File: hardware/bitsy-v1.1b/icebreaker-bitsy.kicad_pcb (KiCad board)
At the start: 4 copper layers, 35.6 x 18 mm, 99 parts, among them J1 USB_C, P0 0, P1 1, P10 10, P11 11, P12 12, P13 13, P14 14, P15 15, P16 16, P17 17, P18 18, P19 19, P2 2, P20 20, P21 21, P22 22, P23 23, P24 GND, P25 GND, P26 GND, P27 3V3, P28 3V3, P29 VIN, P3 3, P30 CDONE, P31 CRESET, P32 UP, P33 UP, P34 UP, P35 UP, P36 CS, P37 SCK, P38 MISO, P39 MOSI, P4 4, P40 IO3, P41 IO2, P5 5, P6 6, P7 7, P8 8, P9 9, SW1 TACT, U1 USBLC6-2, U2 TLV75533PDRV, U3 TLV75512PDRV, U4 LY68L6400, U5 W25Q128JVxxM, U6 ICE40UP5K-SG48, X1 12MHz

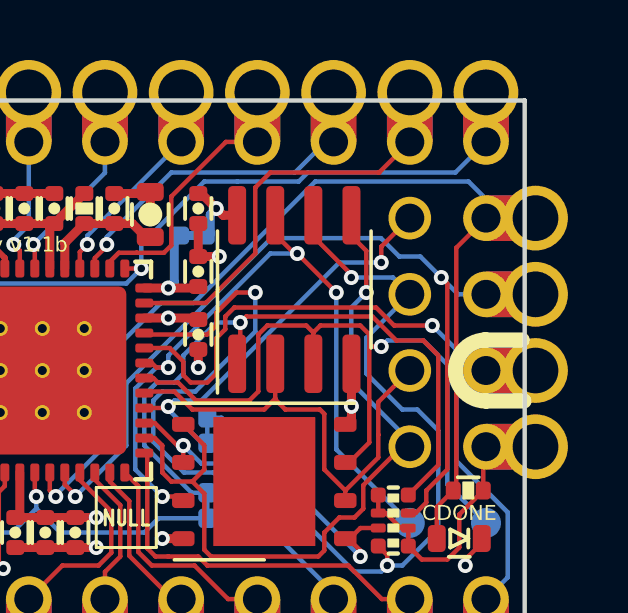
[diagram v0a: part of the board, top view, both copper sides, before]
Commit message: iCEBitsy v1.1b: Add prog header silkscreen labels
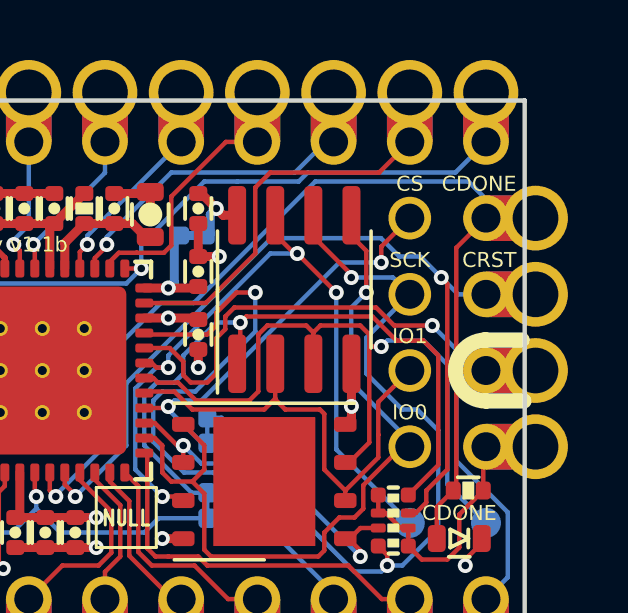
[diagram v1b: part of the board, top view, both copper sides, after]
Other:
- board text added: "CRST"

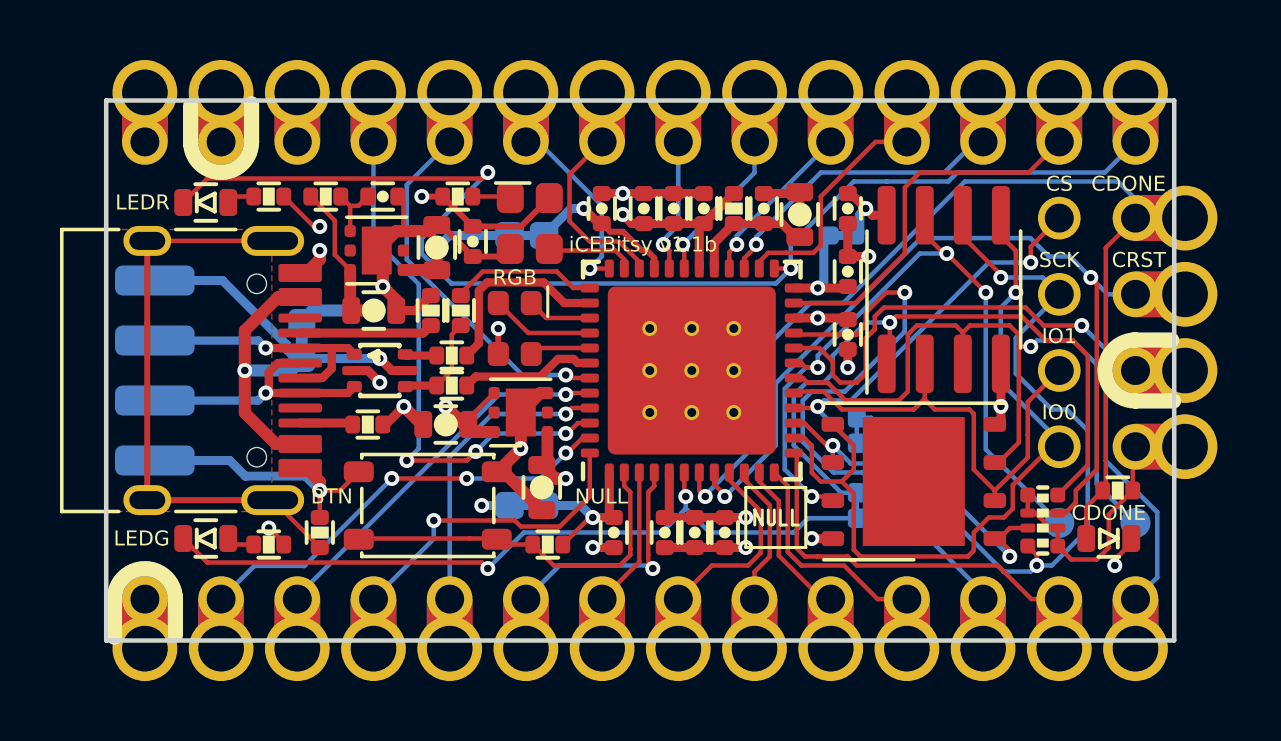
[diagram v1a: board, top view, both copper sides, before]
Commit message: iCEBitsy v1.1b: Change USB paste & add more top silk
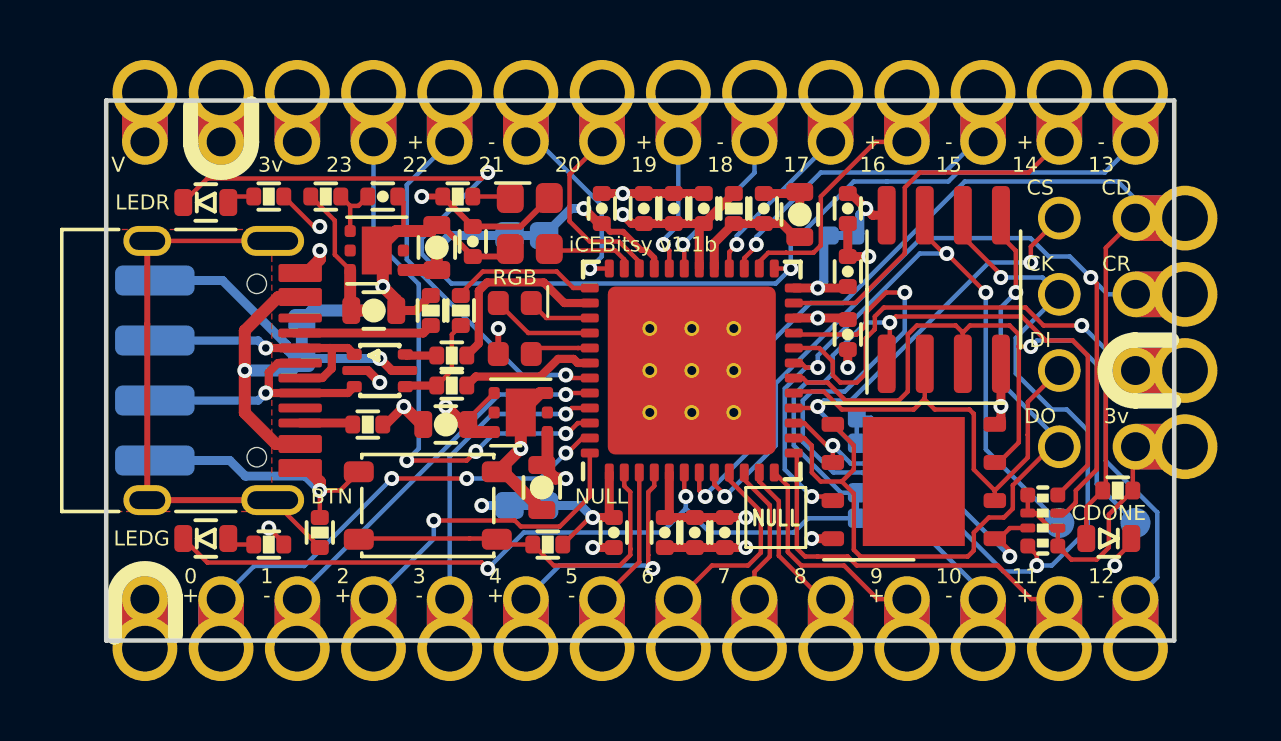
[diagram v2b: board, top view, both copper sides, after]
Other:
- board text added: "3v"
- board text added: "CD"
- board text added: "CK"
- board text added: "CR"
- board text added: "DI"
- board text added: "DO"
- board text removed: "CRST"

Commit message: iCEBitsy v1.1b: Fix grid alignment & finalize board
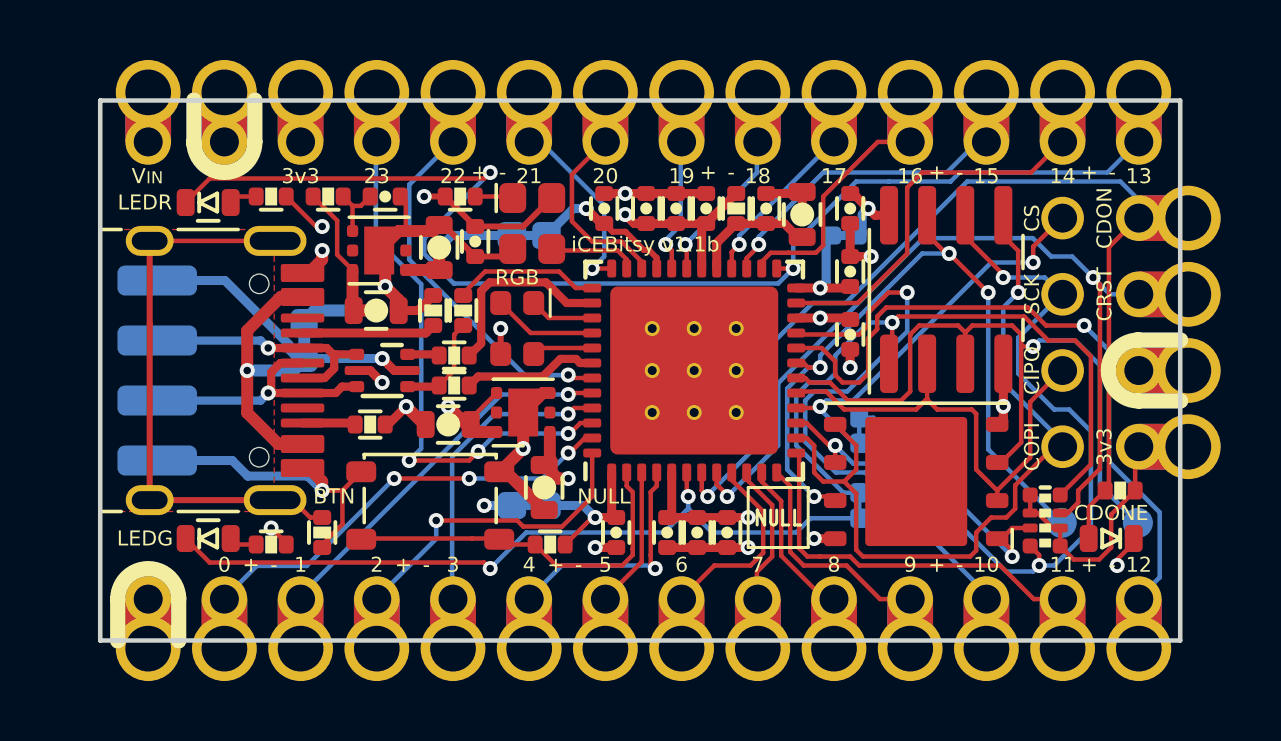
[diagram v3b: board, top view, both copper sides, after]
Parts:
- moved P20 0.11 mm to (48.8, 42.4)
- moved P5 0.11 mm to (48.8, 57.6)
- moved P0 0.11 mm to (36.1, 57.6)
- moved P1 0.11 mm to (38.7, 57.6)
- moved P10 0.11 mm to (61.5, 57.6)
- moved P11 0.11 mm to (64.1, 57.6)
- moved P12 0.11 mm to (66.6, 57.6)
- moved P13 0.11 mm to (66.6, 42.4)
- moved P14 0.11 mm to (64.1, 42.4)
- moved P15 0.11 mm to (61.5, 42.4)
- moved P16 0.11 mm to (59.0, 42.4)
- moved P17 0.11 mm to (56.5, 42.4)
- moved P18 0.11 mm to (53.9, 42.4)
- moved P19 0.11 mm to (51.4, 42.4)
- moved P2 0.11 mm to (41.2, 57.6)
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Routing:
- net GND: track 43.7 -> 45.0 mm
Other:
- board size 35.6 x 18 mm -> 36 x 18 mm
- board text added: "CDON"
- board text added: "CIPO"
- board text added: "COPI"
- board text added: "CRST"
- board text added: "IN"
- board text added: "by Jordi 2020"
- board text removed: "3v"
- board text removed: "CD"
- board text removed: "CK"
- board text removed: "CR"
- board text removed: "DI"
- board text removed: "DO"
- board text removed: "by @0xdec 2020"

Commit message: Updated all design files to KiCad V8.0.6.
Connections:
- net /FLASH_~CS renamed /FLASH_~{CS}
- net /IOB_13b-~LEDG renamed /IOB_13b-~{LEDG}
- net /IOT_36b-~LEDR renamed /IOT_36b-~{LEDR}
- net /RAM_~CS renamed /RAM_~{CS}
- net /SPI_~CS renamed /SPI_~{CS}
- net /SPI_~HLD~-IO3 renamed /SPI_~{HLD}-IO3
- net /SPI_~WP~-IO2 renamed /SPI_~{WP}-IO2
- net /~BTN renamed /~{BTN}
- net /~CRESET renamed /~{CRESET}
- net /~RGB0 renamed /~{RGB0}
- net /~RGB1 renamed /~{RGB1}
- net /~RGB2 renamed /~{RGB2}
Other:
- net class Default removed
- net class S50 removed
- net class USB-D90 removed
- board text added: "13 25 IOT_36b- ~{LEDR}"
- board text added: "~{CRESET}"
- board text added: "~{CS}"
- board text removed: "13 25 IOT_36b- ~LEDR"
- board text removed: "~CRESET"
- board text removed: "~CS"
